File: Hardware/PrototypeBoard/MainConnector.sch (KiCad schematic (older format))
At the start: 2 parts

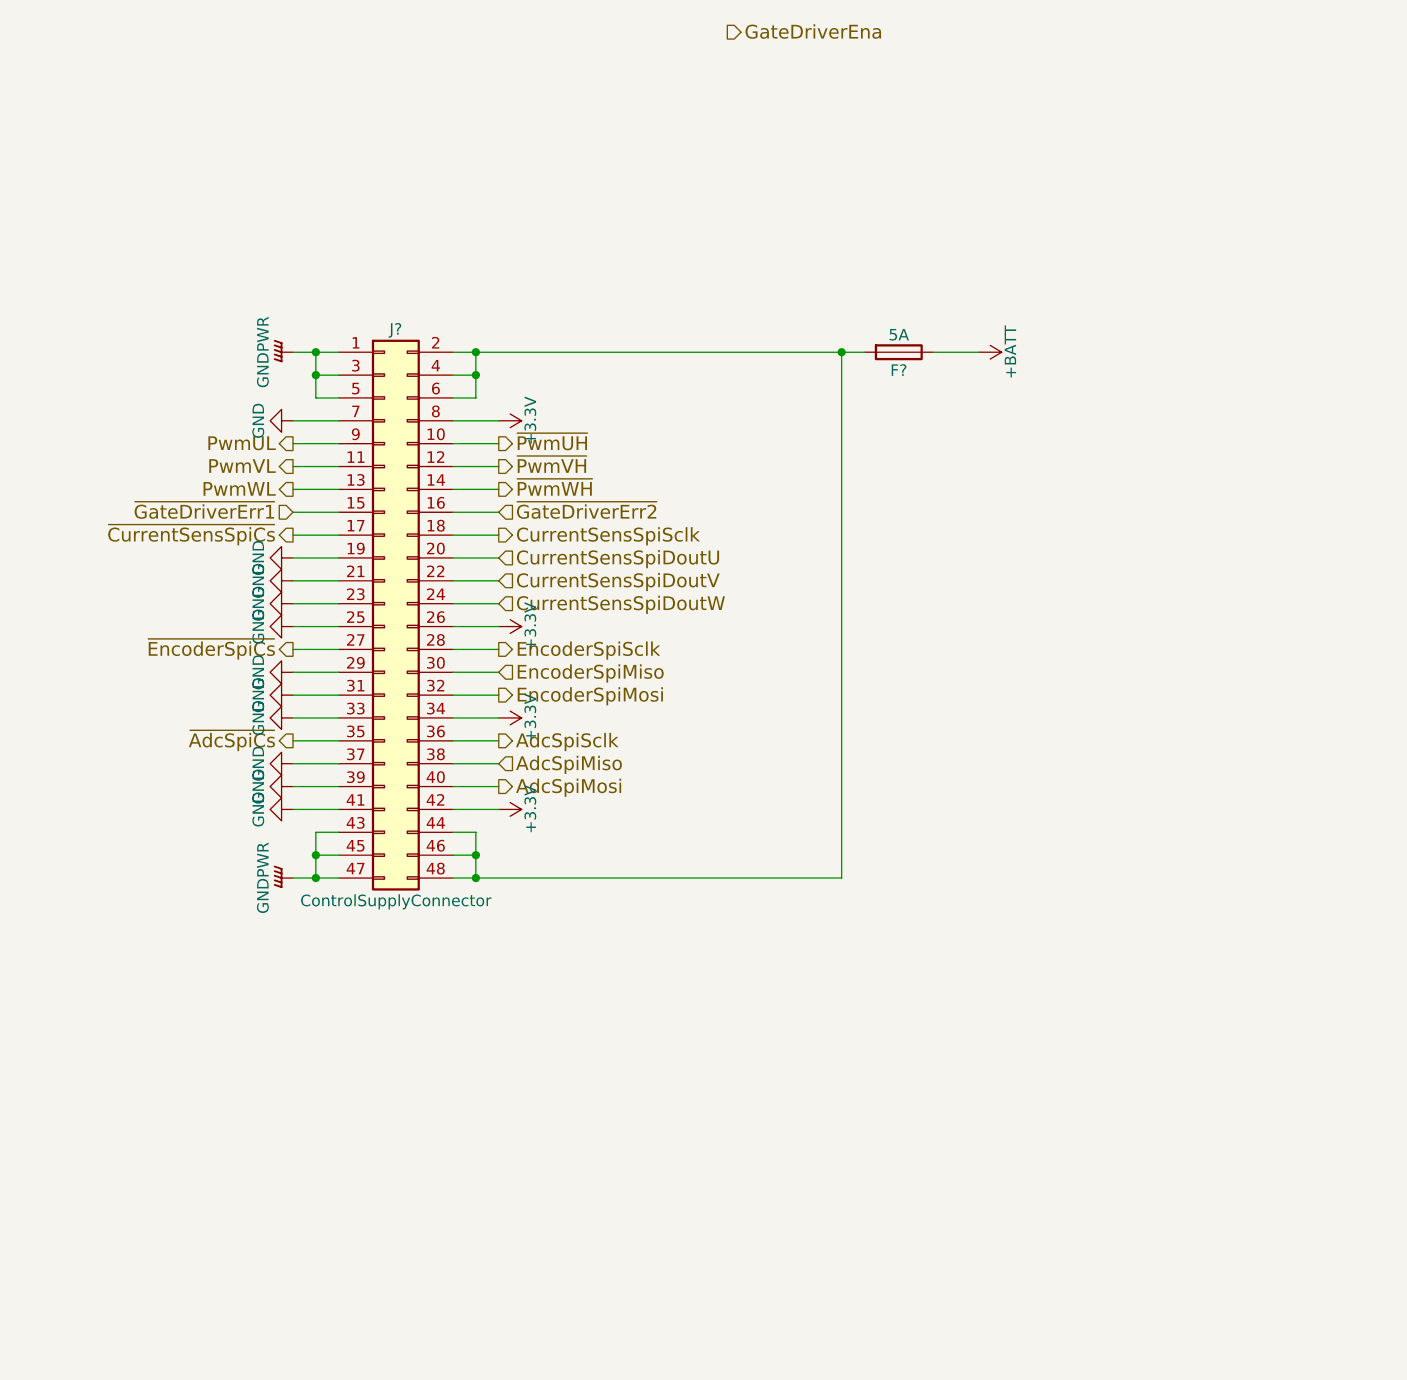
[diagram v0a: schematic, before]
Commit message: Fixed all ERC errors. Added power consumption estimation and other comments. Added links to datasheets. Dimensioned low pass and voltage dividers. Added TVS diodes for protection of voltage rails and ADC inputs. Added fuses. Added Testpoints. Added DC-link capacitors.
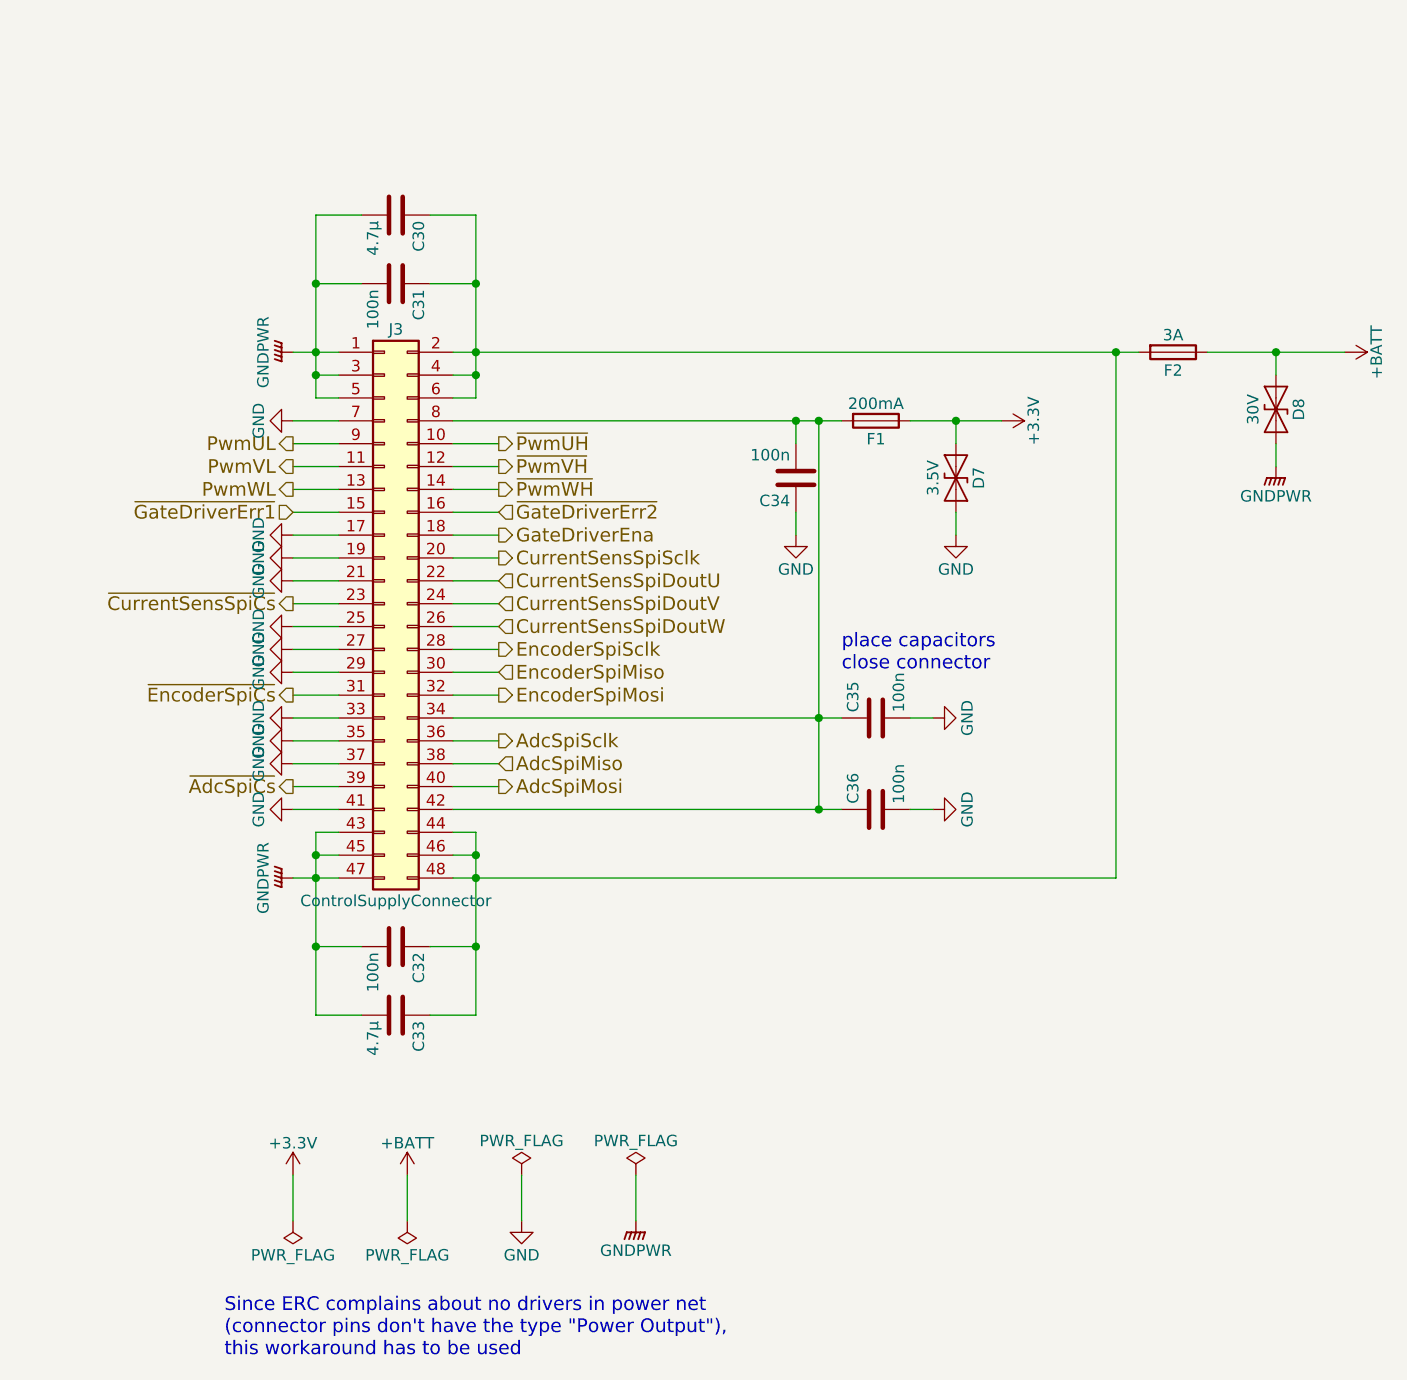
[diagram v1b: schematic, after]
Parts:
- added C30, C33: 4.7μ, symbol C
- added C31, C32, C34, C35, C36: 100n, symbol C
- added D7: 3.5V, symbol D_TVS
- added D8: 30V, symbol D_TVS
- added F1: 200mA, symbol Fuse
- F2: renamed from F?; value 5A -> 3A
- gave numbers to parts that had none: 1
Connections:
- net +3V3: now also D7.1 (A1), F1.1; no longer J3.26 (Pin_26), J3.34 (Pin_34), J3.42 (Pin_42), J3.8 (Pin_8)
- net +BATT: now also D8.1 (A1)
- net CurrentSensSpiDoutU: now also J3.22 (Pin_22); no longer J3.20 (Pin_20)
- net CurrentSensSpiDoutV: now also J3.24 (Pin_24); no longer J3.22 (Pin_22)
- net CurrentSensSpiDoutW: now also J3.26 (Pin_26); no longer J3.24 (Pin_24)
- net CurrentSensSpiSclk: now also J3.20 (Pin_20); no longer J3.18 (Pin_18)
- net GND: now also J3.17 (Pin_17), J3.27 (Pin_27), J3.35 (Pin_35), C34.1, C35.2, C36.2, D7.2 (A2); no longer J3.23 (Pin_23), J3.31 (Pin_31), J3.39 (Pin_39)
- net GNDPWR: now also C30.2, C31.2, C32.2, C33.2, D8.2 (A2)
- net GateDriverEna: now also J3.18 (Pin_18)
- net ~AdcSpiCs: now also J3.39 (Pin_39); no longer J3.35 (Pin_35)
- net ~CurrentSensSpiCs: now also J3.23 (Pin_23); no longer J3.17 (Pin_17)
- net ~EncoderSpiCs: now also J3.31 (Pin_31); no longer J3.27 (Pin_27)
- net at F2.2, J3.2 (Pin_2), J3.4 (Pin_4)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: now also C30.1, C31.1, C32.1, C33.1
- new net: C34.2, C35.1, C36.1, F1.2, J3.34 (Pin_34), J3.42 (Pin_42), J3.8 (Pin_8)
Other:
- note added: "Since ERC complains about no drivers in power net \n(connector pins don't have the type "Power Output"), \nthis workaround has to be used"
- note added: "place capacitors \nclose connector"
- moved on the sheet: F2

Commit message: forgot files
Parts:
- C30, C31, C32, C33, C34, C35, C36: footprint (none) -> Capacitors_SMD:C_0805_HandSoldering
- D7: footprint (none) -> Diodes_SMD:D_SOD-323_HandSoldering
- D8: footprint (none) -> Diodes_SMD:D_SMA-SMB_Universal_Handsoldering
- F1, F2: footprint (none) -> Fuse_Holders_and_Fuses:Fuse_SMD1206_HandSoldering
- J3: footprint (none) -> Pin_Headers:Pin_Header_Straight_2x24_Pitch2.54mm
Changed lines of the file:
@@
 F 0 "J3" H 4050 4600 50  0000 C CNN
 F 1 "ControlSupplyConnector" H 4050 2100 50  0000 C CNN
-F 2 "" H 4000 3400 50  0001 C CNN
+F 2 "Pin_Headers:Pin_Header_Straight_2x24_Pitch2.54mm" H 4000 3400 50  0001 C CNN
 F 3 "" H 4000 3400 50  0001 C CNN
 	1    4000 3400
@@
 F 0 "F2" V 7530 2300 50  0000 C CNN
 F 1 "3A" V 7375 2300 50  0000 C CNN
-F 2 "" V 7380 2300 50  0001 C CNN
+F 2 "Fuse_Holders_and_Fuses:Fuse_SMD1206_HandSoldering" V 7380 2300 50  0001 C CNN
 F 3 "" H 7450 2300 50  0001 C CNN
 	1    7450 2300
@@
 F 0 "C30" H 4075 1800 50  0000 L CNN
 F 1 "4.7μ" H 4075 1600 50  0000 L CNN
-F 2 "" H 4088 1550 50  0001 C CNN
+F 2 "Capacitors_SMD:C_0805_HandSoldering" H 4088 1550 50  0001 C CNN
 F 3 "" H 4050 1700 50  0001 C CNN
 	1    4050 1700
@@
 F 0 "C33" H 4075 5300 50  0000 L CNN
 F 1 "4.7μ" H 4075 5100 50  0000 L CNN
-F 2 "" H 4088 5050 50  0001 C CNN
+F 2 "Capacitors_SMD:C_0805_HandSoldering" H 4088 5050 50  0001 C CNN
 F 3 "" H 4050 5200 50  0001 C CNN
 	1    4050 5200
@@
 F 0 "F1" V 6230 2600 50  0000 C CNN
 F 1 "200mA" V 6075 2600 50  0000 C CNN
-F 2 "" V 6080 2600 50  0001 C CNN
+F 2 "Fuse_Holders_and_Fuses:Fuse_SMD1206_HandSoldering" V 6080 2600 50  0001 C CNN
 F 3 "" H 6150 2600 50  0001 C CNN
 	1    6150 2600
@@
 F 0 "D8" H 7900 2650 50  0000 C CNN
 F 1 "30V" H 7900 2450 50  0000 C CNN
-F 2 "" H 7900 2550 50  0001 C CNN
+F 2 "Diodes_SMD:D_SMA-SMB_Universal_Handsoldering" H 7900 2550 50  0001 C CNN
 F 3 "" H 7900 2550 50  0001 C CNN
 	1    7900 2550
@@
 F 0 "D7" H 6500 2950 50  0000 C CNN
 F 1 "3.5V" H 6500 2750 50  0000 C CNN
-F 2 "" H 6500 2850 50  0001 C CNN
+F 2 "Diodes_SMD:D_SOD-323_HandSoldering" H 6500 2850 50  0001 C CNN
 F 3 "" H 6500 2850 50  0001 C CNN
 	1    6500 2850
@@
 F 0 "C32" H 4075 5000 50  0000 L CNN
 F 1 "100n" H 4075 4800 50  0000 L CNN
-F 2 "" H 4088 4750 50  0001 C CNN
+F 2 "Capacitors_SMD:C_0805_HandSoldering" H 4088 4750 50  0001 C CNN
 F 3 "" H 4050 4900 50  0001 C CNN
 	1    4050 4900
@@
 F 0 "C31" H 4075 2100 50  0000 L CNN
 F 1 "100n" H 4075 1900 50  0000 L CNN
-F 2 "" H 4088 1850 50  0001 C CNN
+F 2 "Capacitors_SMD:C_0805_HandSoldering" H 4088 1850 50  0001 C CNN
 F 3 "" H 4050 2000 50  0001 C CNN
 	1    4050 2000
@@
 F 0 "C34" H 5825 2950 50  0000 L CNN
 F 1 "100n" H 5825 2750 50  0000 L CNN
-F 2 "" H 5838 2700 50  0001 C CNN
+F 2 "Capacitors_SMD:C_0805_HandSoldering" H 5838 2700 50  0001 C CNN
 F 3 "" H 5800 2850 50  0001 C CNN
 	1    5800 2850
@@
 F 0 "C35" H 6175 4000 50  0000 L CNN
 F 1 "100n" H 6175 3800 50  0000 L CNN
-F 2 "" H 6188 3750 50  0001 C CNN
+F 2 "Capacitors_SMD:C_0805_HandSoldering" H 6188 3750 50  0001 C CNN
 F 3 "" H 6150 3900 50  0001 C CNN
 	1    6150 3900
@@
 F 0 "C36" H 6175 4400 50  0000 L CNN
 F 1 "100n" H 6175 4200 50  0000 L CNN
-F 2 "" H 6188 4150 50  0001 C CNN
+F 2 "Capacitors_SMD:C_0805_HandSoldering" H 6188 4150 50  0001 C CNN
 F 3 "" H 6150 4300 50  0001 C CNN
 	1    6150 4300

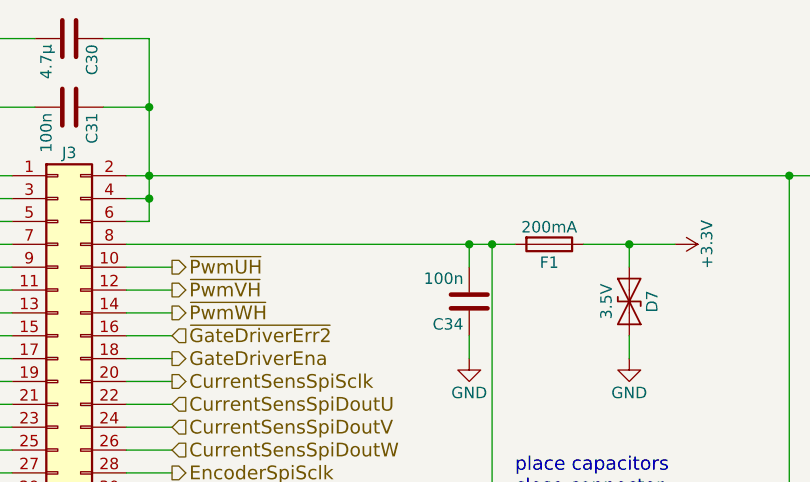
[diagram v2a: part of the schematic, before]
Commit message: assigned net classes and a few net names
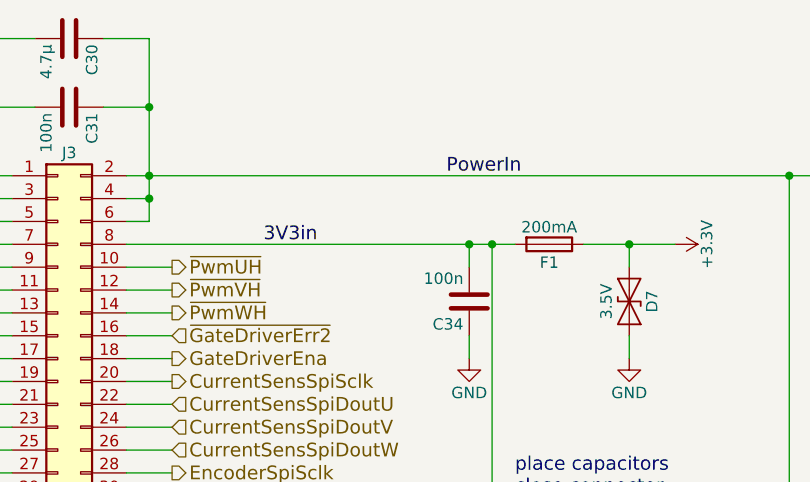
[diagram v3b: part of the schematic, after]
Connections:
- net PowerIn: now reaches C30.1, C31.1, C32.1, C33.1, F2.2, J3.2 (Pin_2), J3.4 (Pin_4), J3.44 (Pin_44), J3.46 (Pin_46), J3.48 (Pin_48), J3.6 (Pin_6)
- net 3V3in: now reaches C34.2, C35.1, C36.1, F1.2, J3.34 (Pin_34), J3.42 (Pin_42), J3.8 (Pin_8)
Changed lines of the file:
@@
 Text Notes 6000 3700 0    60   ~ 0
 place capacitors \nclose connector
+Text Label 5700 2300 0    60   ~ 0
+PowerIn
+Text Label 4900 2600 0    60   ~ 0
+3V3in
 $EndSCHEMATC

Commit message: some more layout...
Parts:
- renumbered C30 to C33, C31 to C34, C32 to C35, C33 to C36, C34 to C37, C35 to C38, C36 to C39
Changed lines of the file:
@@
 	3600 3100 3800 3100
 $Comp
-L C C30
+L C C33
 U 1 1 5AFF8734
 P 4050 1700
-F 0 "C30" H 4075 1800 50  0000 L CNN
+F 0 "C33" H 4075 1800 50  0000 L CNN
 F 1 "4.7μ" H 4075 1600 50  0000 L CNN
 F 2 "Capacitors_SMD:C_0805_HandSoldering" H 4088 1550 50  0001 C CNN
@@
 $EndComp
 $Comp
-L C C33
+L C C36
 U 1 1 5AFF8906
 P 4050 5200
-F 0 "C33" H 4075 5300 50  0000 L CNN
+F 0 "C36" H 4075 5300 50  0000 L CNN
 F 1 "4.7μ" H 4075 5100 50  0000 L CNN
 F 2 "Capacitors_SMD:C_0805_HandSoldering" H 4088 5050 50  0001 C CNN
@@
 Connection ~ 6500 2600
 $Comp
-L C C32
+L C C35
 U 1 1 5B00D7DF
 P 4050 4900
-F 0 "C32" H 4075 5000 50  0000 L CNN
+F 0 "C35" H 4075 5000 50  0000 L CNN
 F 1 "100n" H 4075 4800 50  0000 L CNN
 F 2 "Capacitors_SMD:C_0805_HandSoldering" H 4088 4750 50  0001 C CNN
@@
 Connection ~ 3700 4900
 $Comp
-L C C31
+L C C34
 U 1 1 5B00D9FF
 P 4050 2000
-F 0 "C31" H 4075 2100 50  0000 L CNN
+F 0 "C34" H 4075 2100 50  0000 L CNN
 F 1 "100n" H 4075 1900 50  0000 L CNN
 F 2 "Capacitors_SMD:C_0805_HandSoldering" H 4088 1850 50  0001 C CNN
@@
 Connection ~ 4400 2000
 $Comp
-L C C34
+L C C37
 U 1 1 5B00DC69
 P 5800 2850
-F 0 "C34" H 5825 2950 50  0000 L CNN
+F 0 "C37" H 5825 2950 50  0000 L CNN
 F 1 "100n" H 5825 2750 50  0000 L CNN
 F 2 "Capacitors_SMD:C_0805_HandSoldering" H 5838 2700 50  0001 C CNN
@@
 $EndComp
 $Comp
-L C C35
+L C C38
 U 1 1 5B00DD38
 P 6150 3900
-F 0 "C35" H 6175 4000 50  0000 L CNN
+F 0 "C38" H 6175 4000 50  0000 L CNN
 F 1 "100n" H 6175 3800 50  0000 L CNN
 F 2 "Capacitors_SMD:C_0805_HandSoldering" H 6188 3750 50  0001 C CNN
@@
 $EndComp
 $Comp
-L C C36
+L C C39
 U 1 1 5B00DD8B
 P 6150 4300
-F 0 "C36" H 6175 4400 50  0000 L CNN
+F 0 "C39" H 6175 4400 50  0000 L CNN
 F 1 "100n" H 6175 4200 50  0000 L CNN
 F 2 "Capacitors_SMD:C_0805_HandSoldering" H 6188 4150 50  0001 C CNN

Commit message: more layout and some changes to schematic
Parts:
- J3: footprint Pin_Headers:Pin_Header_Straight_2x24_Pitch2.54mm -> Pin_Headers:Pin_Header_Straight_2x24_Pitch2.00mm
- renumbered C33 to C34, C34 to C35, C35 to C36, C36 to C37, C37 to C38, C38 to C39, C39 to C40
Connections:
- net GND: now also J3.11 (Pin_11); no longer J3.17 (Pin_17)
- net GateDriverEna: now also J3.12 (Pin_12); no longer J3.18 (Pin_18)
- net PwmUL: now also J3.13 (Pin_13); no longer J3.9 (Pin_9)
- net PwmVL: now also J3.15 (Pin_15); no longer J3.11 (Pin_11)
- net PwmWL: now also J3.17 (Pin_17); no longer J3.13 (Pin_13)
- net ~GateDriverErr1: now also J3.10 (Pin_10); no longer J3.15 (Pin_15)
- net ~GateDriverErr2: now also J3.9 (Pin_9); no longer J3.16 (Pin_16)
- net ~PwmUH: now also J3.14 (Pin_14); no longer J3.10 (Pin_10)
- net ~PwmVH: now also J3.16 (Pin_16); no longer J3.12 (Pin_12)
- net ~PwmWH: now also J3.18 (Pin_18); no longer J3.14 (Pin_14)

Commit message: More Layout...
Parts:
- added D8: 30V, Diodes_SMD:D_SMA-SMB_Universal_Handsoldering, symbol D_TVS
- renumbered D8 to D9
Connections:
- net GNDPWR: now also D8.2 (A2)
- net PowerIn: now also D8.1 (A1)
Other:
- note added: "TVS diode at \nthe PowerIn net\nburns the fuse in case \nDC link voltage rises \nover 30V during \nregenerative breaking"
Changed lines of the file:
@@
 	4400 2500 4300 2500
-Wire Wire Line
-	4300 2300 7300 2300
 Wire Wire Line
 	4300 2400 4400 2400
@@
 $EndComp
 $Comp
-L D_TVS D8
+L D_TVS D9
 U 1 1 5B00D2A4
 P 7900 2550
-F 0 "D8" H 7900 2650 50  0000 C CNN
+F 0 "D9" H 7900 2650 50  0000 C CNN
 F 1 "30V" H 7900 2450 50  0000 C CNN
 F 2 "Diodes_SMD:D_SMA-SMB_Universal_Handsoldering" H 7900 2550 50  0001 C CNN
@@
 Text Label 4900 2600 0    60   ~ 0
 3V3in
+$Comp
+L D_TVS D8
+U 1 1 5B27A7EB
+P 7000 2450
+F 0 "D8" H 7000 2550 50  0000 C CNN
+F 1 "30V" H 7000 2350 50  0000 C CNN
+F 2 "Diodes_SMD:D_SMA-SMB_Universal_Handsoldering" H 7000 2450 50  0001 C CNN
+F 3 "" H 7000 2450 50  0001 C CNN
+	1    7000 2450
+	0    1    1    0
+$EndComp
+Wire Wire Line
+	4300 2300 7300 2300
+Connection ~ 7000 2300
+$Comp
+L GNDPWR #PWR097
+U 1 1 5B27AA44
+P 7000 2650
+F 0 "#PWR097" H 7000 2450 50  0001 C CNN
+F 1 "GNDPWR" H 7000 2520 50  0000 C CNN
+F 2 "" H 7000 2600 50  0001 C CNN
+F 3 "" H 7000 2600 50  0001 C CNN
+	1    7000 2650
+	1    0    0    -1
+$EndComp
+Wire Wire Line
+	7000 2650 7000 2600
+Text Notes 6550 2150 0    60   ~ 0
+TVS diode at \nthe PowerIn net\nburns the fuse in case \nDC link voltage rises \nover 30V during \nregenerative breaking
 $EndSCHEMATC

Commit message: layout and some pin swapping...
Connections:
- net CurrentSensSpiDoutU: now also J3.26 (Pin_26); no longer J3.22 (Pin_22)
- net CurrentSensSpiDoutW: now also J3.22 (Pin_22); no longer J3.26 (Pin_26)
- net GND: now also J3.23 (Pin_23); no longer J3.21 (Pin_21)
- net ~CurrentSensSpiCs: now also J3.21 (Pin_21); no longer J3.23 (Pin_23)
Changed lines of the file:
@@
 Text HLabel 4500 4200 2    60   Output ~ 0
 AdcSpiMosi
-Text HLabel 3600 3400 0    60   Output ~ 0
+Text HLabel 3600 3300 0    60   Output ~ 0
 ~CurrentSensSpiCs
 Text HLabel 4500 2800 2    60   Output ~ 0
@@
 Text HLabel 4500 3200 2    60   Output ~ 0
 CurrentSensSpiSclk
-Text HLabel 4500 3300 2    60   Input ~ 0
+Text HLabel 4500 3500 2    60   Input ~ 0
 CurrentSensSpiDoutU
 Text HLabel 4500 3400 2    60   Input ~ 0
 CurrentSensSpiDoutV
-Text HLabel 4500 3500 2    60   Input ~ 0
+Text HLabel 4500 3300 2    60   Input ~ 0
 CurrentSensSpiDoutW
 $Comp
@@
 L GND #PWR081
 U 1 1 5AFFCAA6
-P 3600 3300
-F 0 "#PWR081" H 3600 3050 50  0001 C CNN
-F 1 "GND" H 3600 3150 50  0000 C CNN
-F 2 "" H 3600 3300 50  0001 C CNN
-F 3 "" H 3600 3300 50  0001 C CNN
-	1    3600 3300
+P 3600 3400
+F 0 "#PWR081" H 3600 3150 50  0001 C CNN
+F 1 "GND" H 3600 3250 50  0000 C CNN
+F 2 "" H 3600 3400 50  0001 C CNN
+F 3 "" H 3600 3400 50  0001 C CNN
+	1    3600 3400
 	0    1    1    0
 $EndComp
